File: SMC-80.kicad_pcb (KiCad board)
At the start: 4 copper layers, 101.6 x 102.1 mm, 109 parts, among them J1 RC80 Bus, J10 Jack-DC, J11 USB_B_Micro, J2 RC80 Expansion, J3 PMOD, J4 JTAG, J5 PIO Header, J6 Port A, J7 Port A, J8 SIO CLK SEL, J9 IDE, SW1 Reset, SW2 User PB, SW3 User DIP, U1 DS1813R-5+T&R, U10 SST39SF040, U11 AZ2940-5.0, U12 MAX40203AUK, U13 LP2985-3.3, U14 MAX40203AUK, U2 TXS0108EPW, U3 74LVC1G04, U4 EPM7064STC100, U5 Z84C4310AEG, U6 Z84C2010AEG, U7 Z84C3010AEG, U8 AS6C4008A-55ZIN, U9 Z84C0010AEG, X1 CFPS-72 50mhz

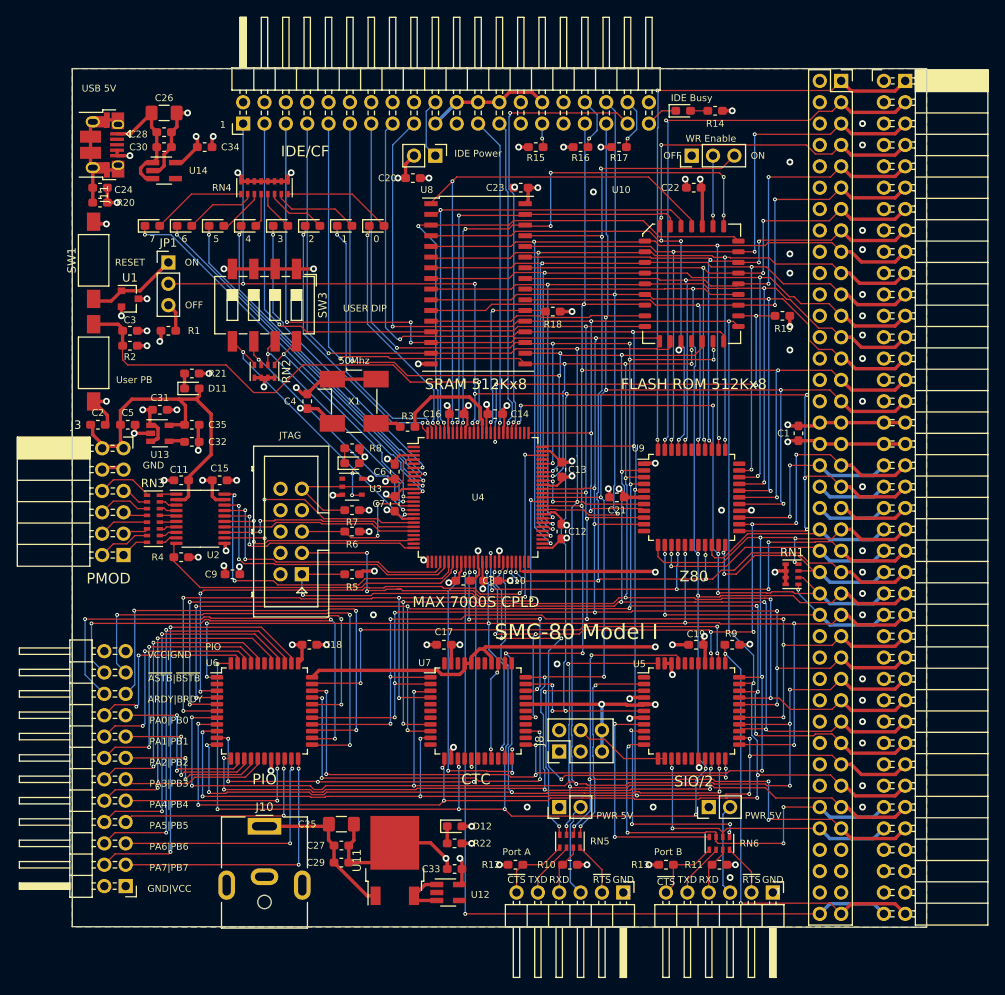
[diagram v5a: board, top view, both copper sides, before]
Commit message: Changed 5V regulator, added additional SS text
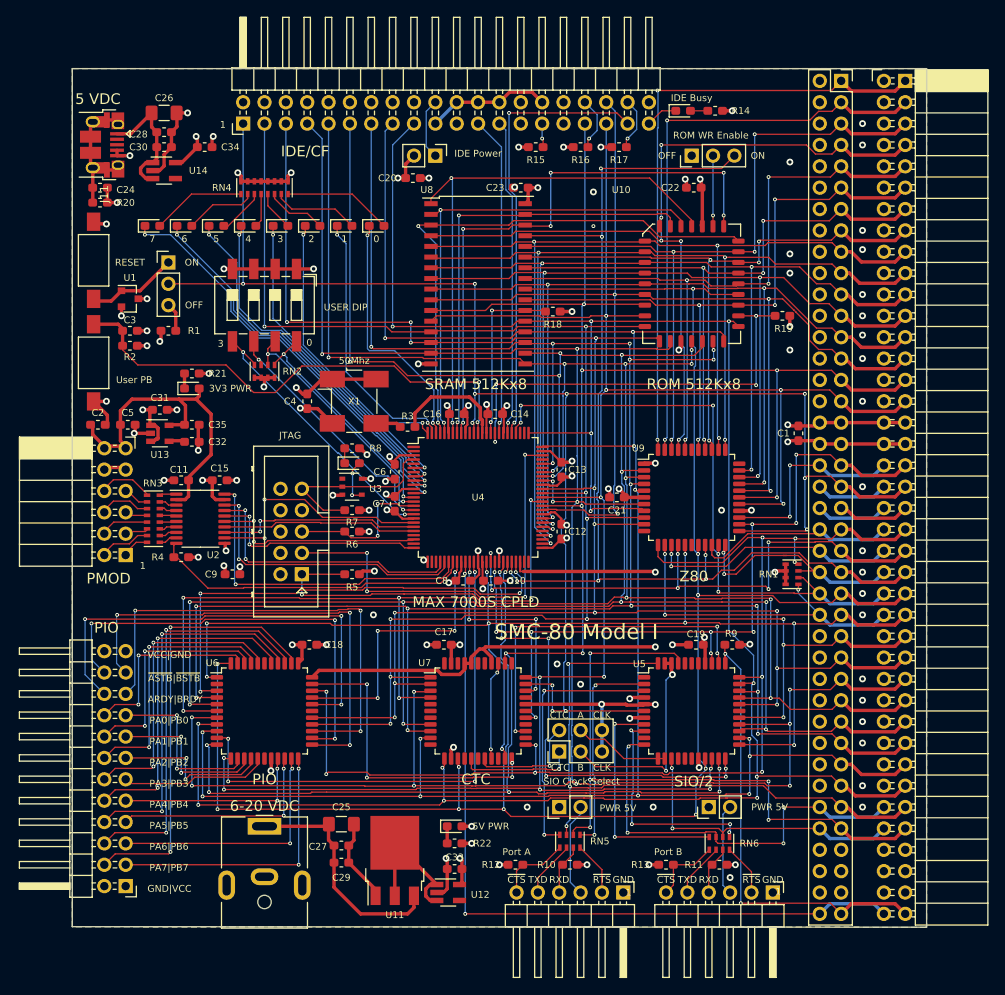
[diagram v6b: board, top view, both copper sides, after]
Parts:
- U11: value AZ2940-5.0 -> AZ1117-5.0; footprint Package_TO_SOT_SMD:TO-252-2 -> Package_TO_SOT_SMD:TO-252-3_TabPin2
- moved J3 0.25 mm to (108.0, 76.7)
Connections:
- J1 pad 10: (no net) -> Net-(J1-Pad10)
- J1 pad 12: (no net) -> Net-(J1-Pad12)
- J1 pad 14: (no net) -> Net-(J1-Pad14)
- J1 pad 16: (no net) -> Net-(J1-Pad16)
- J1 pad 18: (no net) -> Net-(J1-Pad18)
- J1 pad 2: (no net) -> Net-(J1-Pad2)
- J1 pad 20: (no net) -> Net-(J1-Pad20)
- J1 pad 22: (no net) -> Net-(J1-Pad22)
- J1 pad 24: (no net) -> Net-(J1-Pad24)
- J1 pad 26: (no net) -> Net-(J1-Pad26)
- J1 pad 28: (no net) -> Net-(J1-Pad28)
- J1 pad 30: (no net) -> Net-(J1-Pad30)
- J1 pad 32: (no net) -> Net-(J1-Pad32)
- J1 pad 4: (no net) -> Net-(J1-Pad4)
- J1 pad 54: (no net) -> Net-(J1-Pad54)
- J1 pad 56: (no net) -> Net-(J1-Pad56)
- J1 pad 58: (no net) -> Net-(J1-Pad58)
- J1 pad 6: (no net) -> Net-(J1-Pad6)
- J1 pad 60: (no net) -> Net-(J1-Pad60)
- J1 pad 62: (no net) -> Net-(J1-Pad62)
- J1 pad 64: (no net) -> Net-(J1-Pad64)
- J1 pad 66: (no net) -> Net-(J1-Pad66)
- J1 pad 68: (no net) -> Net-(J1-Pad68)
- J1 pad 73: (no net) -> Net-(J1-Pad73)
- J1 pad 74: (no net) -> Net-(J1-Pad74)
- J1 pad 75: (no net) -> Net-(J1-Pad75)
- J1 pad 76: (no net) -> Net-(J1-Pad76)
- J1 pad 77: (no net) -> Net-(J1-Pad77)
- J1 pad 78: (no net) -> Net-(J1-Pad78)
- J1 pad 8: (no net) -> Net-(J1-Pad8)
- J11 pad 2: (no net) -> Net-(J11-Pad2)
- J11 pad 3: (no net) -> Net-(J11-Pad3)
- J2 pad 10: (no net) -> Net-(J2-Pad10)
- J2 pad 12: (no net) -> Net-(J2-Pad12)
- J2 pad 14: (no net) -> Net-(J2-Pad14)
- J2 pad 16: (no net) -> Net-(J2-Pad16)
- J2 pad 18: (no net) -> Net-(J2-Pad18)
- J2 pad 2: (no net) -> Net-(J2-Pad2)
- J2 pad 20: (no net) -> Net-(J2-Pad20)
- J2 pad 22: (no net) -> Net-(J2-Pad22)
- J2 pad 24: (no net) -> Net-(J2-Pad24)
- J2 pad 26: (no net) -> Net-(J2-Pad26)
- J2 pad 28: (no net) -> Net-(J2-Pad28)
- J2 pad 30: (no net) -> Net-(J2-Pad30)
- J2 pad 32: (no net) -> Net-(J2-Pad32)
- J2 pad 4: (no net) -> Net-(J2-Pad4)
- J2 pad 54: (no net) -> Net-(J2-Pad54)
- J2 pad 56: (no net) -> Net-(J2-Pad56)
- J2 pad 58: (no net) -> Net-(J2-Pad58)
- J2 pad 6: (no net) -> Net-(J2-Pad6)
- J2 pad 60: (no net) -> Net-(J2-Pad60)
- J2 pad 62: (no net) -> Net-(J2-Pad62)
- J2 pad 64: (no net) -> Net-(J2-Pad64)
- J2 pad 66: (no net) -> Net-(J2-Pad66)
- J2 pad 68: (no net) -> Net-(J2-Pad68)
- J2 pad 73: (no net) -> Net-(J2-Pad73)
- J2 pad 74: (no net) -> Net-(J2-Pad74)
- J2 pad 75: (no net) -> Net-(J2-Pad75)
- J2 pad 76: (no net) -> Net-(J2-Pad76)
- J2 pad 77: (no net) -> Net-(J2-Pad77)
- J2 pad 78: (no net) -> Net-(J2-Pad78)
- J2 pad 8: (no net) -> Net-(J2-Pad8)
- J4 pad 6: (no net) -> Net-(J4-Pad6)
- J4 pad 7: (no net) -> Net-(J4-Pad7)
- J4 pad 8: (no net) -> Net-(J4-Pad8)
- J9 pad 10: (no net) -> Net-(J9-Pad10)
- J9 pad 12: (no net) -> Net-(J9-Pad12)
- J9 pad 14: (no net) -> Net-(J9-Pad14)
- J9 pad 16: (no net) -> Net-(J9-Pad16)
- J9 pad 18: (no net) -> Net-(J9-Pad18)
- J9 pad 21: (no net) -> Net-(J9-Pad21)
- J9 pad 27: (no net) -> Net-(J9-Pad27)
- J9 pad 28: (no net) -> Net-(J9-Pad28)
- J9 pad 31: (no net) -> Net-(J9-Pad31)
- J9 pad 32: (no net) -> Net-(J9-Pad32)
- J9 pad 4: (no net) -> Net-(J9-Pad4)
- J9 pad 6: (no net) -> Net-(J9-Pad6)
- J9 pad 8: (no net) -> Net-(J9-Pad8)
- U11 pad 1: Net-(C25-Pad1) -> GND
- U11 pad 2: GND -> Net-(U11-Pad2)
- U11 pad 3: Net-(U11-Pad3) -> Net-(C25-Pad1)
- U12 pad 1: Net-(U11-Pad3) -> Net-(U11-Pad2)
- U12 pad 3: Net-(U11-Pad3) -> Net-(U11-Pad2)
- U12 pad 4: (no net) -> Net-(U12-Pad4)
- U14 pad 4: (no net) -> Net-(U14-Pad4)
- U4 pad 1: (no net) -> Net-(U4-Pad1)
- U4 pad 2: (no net) -> Net-(U4-Pad2)
- U4 pad 22: (no net) -> Net-(U4-Pad22)
- U4 pad 24: (no net) -> Net-(U4-Pad24)
- U4 pad 27: (no net) -> Net-(U4-Pad27)
- U4 pad 28: (no net) -> Net-(U4-Pad28)
- U4 pad 49: (no net) -> Net-(U4-Pad49)
- U4 pad 5: (no net) -> Net-(U4-Pad5)
- U4 pad 50: (no net) -> Net-(U4-Pad50)
- U4 pad 53: (no net) -> Net-(U4-Pad53)
- U4 pad 55: (no net) -> Net-(U4-Pad55)
- U4 pad 7: (no net) -> Net-(U4-Pad7)
- U4 pad 70: (no net) -> Net-(U4-Pad70)
- U4 pad 72: (no net) -> Net-(U4-Pad72)
- U4 pad 77: (no net) -> Net-(U4-Pad77)
- U4 pad 78: (no net) -> Net-(U4-Pad78)
- U4 pad 90: (no net) -> Net-(U4-Pad90)
- U5 pad 1: (no net) -> Net-(U5-Pad1)
- U5 pad 10: (no net) -> Net-(U5-Pad10)
- U5 pad 15: (no net) -> Net-(U5-Pad15)
- U5 pad 16: (no net) -> Net-(U5-Pad16)
- U5 pad 17: (no net) -> Net-(U5-Pad17)
- U5 pad 28: (no net) -> Net-(U5-Pad28)
- U5 pad 38: (no net) -> Net-(U5-Pad38)
- U5 pad 39: (no net) -> Net-(U5-Pad39)
- U5 pad 40: (no net) -> Net-(U5-Pad40)
- U6 pad 2: (no net) -> Net-(U6-Pad2)
- U6 pad 28: (no net) -> Net-(U6-Pad28)
- U6 pad 39: (no net) -> Net-(U6-Pad39)
- U7 pad 11: (no net) -> Net-(U7-Pad11)
- U7 pad 15: (no net) -> Net-(U7-Pad15)
- U7 pad 17: (no net) -> Net-(U7-Pad17)
- U7 pad 20: (no net) -> Net-(U7-Pad20)
- U7 pad 24: (no net) -> Net-(U7-Pad24)
- U7 pad 26: (no net) -> Net-(U7-Pad26)
- U7 pad 28: (no net) -> Net-(U7-Pad28)
- U7 pad 30: (no net) -> Net-(U7-Pad30)
- U7 pad 34: (no net) -> Net-(U7-Pad34)
- U7 pad 38: (no net) -> Net-(U7-Pad38)
- U7 pad 39: (no net) -> Net-(U7-Pad39)
- U7 pad 42: (no net) -> Net-(U7-Pad42)
- U7 pad 44: (no net) -> Net-(U7-Pad44)
- U7 pad 5: (no net) -> Net-(U7-Pad5)
- U7 pad 6: (no net) -> Net-(U7-Pad6)
- U7 pad 7: (no net) -> Net-(U7-Pad7)
- U9 pad 11: (no net) -> Net-(U9-Pad11)
- U9 pad 17: (no net) -> Net-(U9-Pad17)
- U9 pad 33: (no net) -> Net-(U9-Pad33)
- U9 pad 39: (no net) -> Net-(U9-Pad39)
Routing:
- net /CLK2: track 38.0 -> 60.9 mm, vias 1 -> 2
- net Net-(U11-Pad2): track 0.00 -> 17.3 mm
- net /Peripherals/IEO_0: track 59.2 -> 42.0 mm
- net /Peripherals/TO_1: track 0.00 -> 13.3 mm, vias 0 -> 1
- net /Peripherals/TO_0: track 1.01 -> 13.8 mm
- net Net-(C25-Pad1): track 19.2 -> 28.1 mm
- net /Peripherals/IEO_1: track 44.3 -> 37.4 mm
- net Net-(U11-Pad3): track 6.23 -> 0.00 mm
- net GND: track 159.4 -> 155.5 mm, vias 84 -> 86
- net /IEO_2: track 36.9 -> 33.3 mm
- net /CPLD/LED6: track 44.2 -> 46.2 mm
- net /CPLD/LED7: track 48.4 -> 50.3 mm
- net /SIO_~CE: track 57.0 -> 55.2 mm
- net /CPLD/LED5: track 42.0 -> 43.7 mm
- net /CPLD/LED0: track 28.2 -> 30.0 mm
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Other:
- board text added: "3V3 PWR"
- board text added: "5 VDC"
- board text added: "5V PWR"
- board text added: "6-20 VDC"
- board text added: "A"
- board text added: "B"
- board text added: "CLK"
- board text added: "ROM 512Kx8"
- board text added: "ROM WR Enable"
- board text added: "SIO Clock Select"
- board text removed: "FLASH ROM 512Kx8"
- board text removed: "USB 5V"
- board text removed: "WR Enable"
